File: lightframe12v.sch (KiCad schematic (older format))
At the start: 43 parts, among them J1 PJ-077, J2 Conn_01x06_Female, J3 Conn_01x02_Female, J4 Conn_01x06_Female, J5 Conn_01x04_Female, J6 Conn_01x6_Female, Q1 MMBT2222A-TP, Q2 MMBT2222A-TP, SW1 SW_Push, SW2 SW_Push, U1 TPS562211, U2 ESP32-WROOM-32U, U3 TLC5971

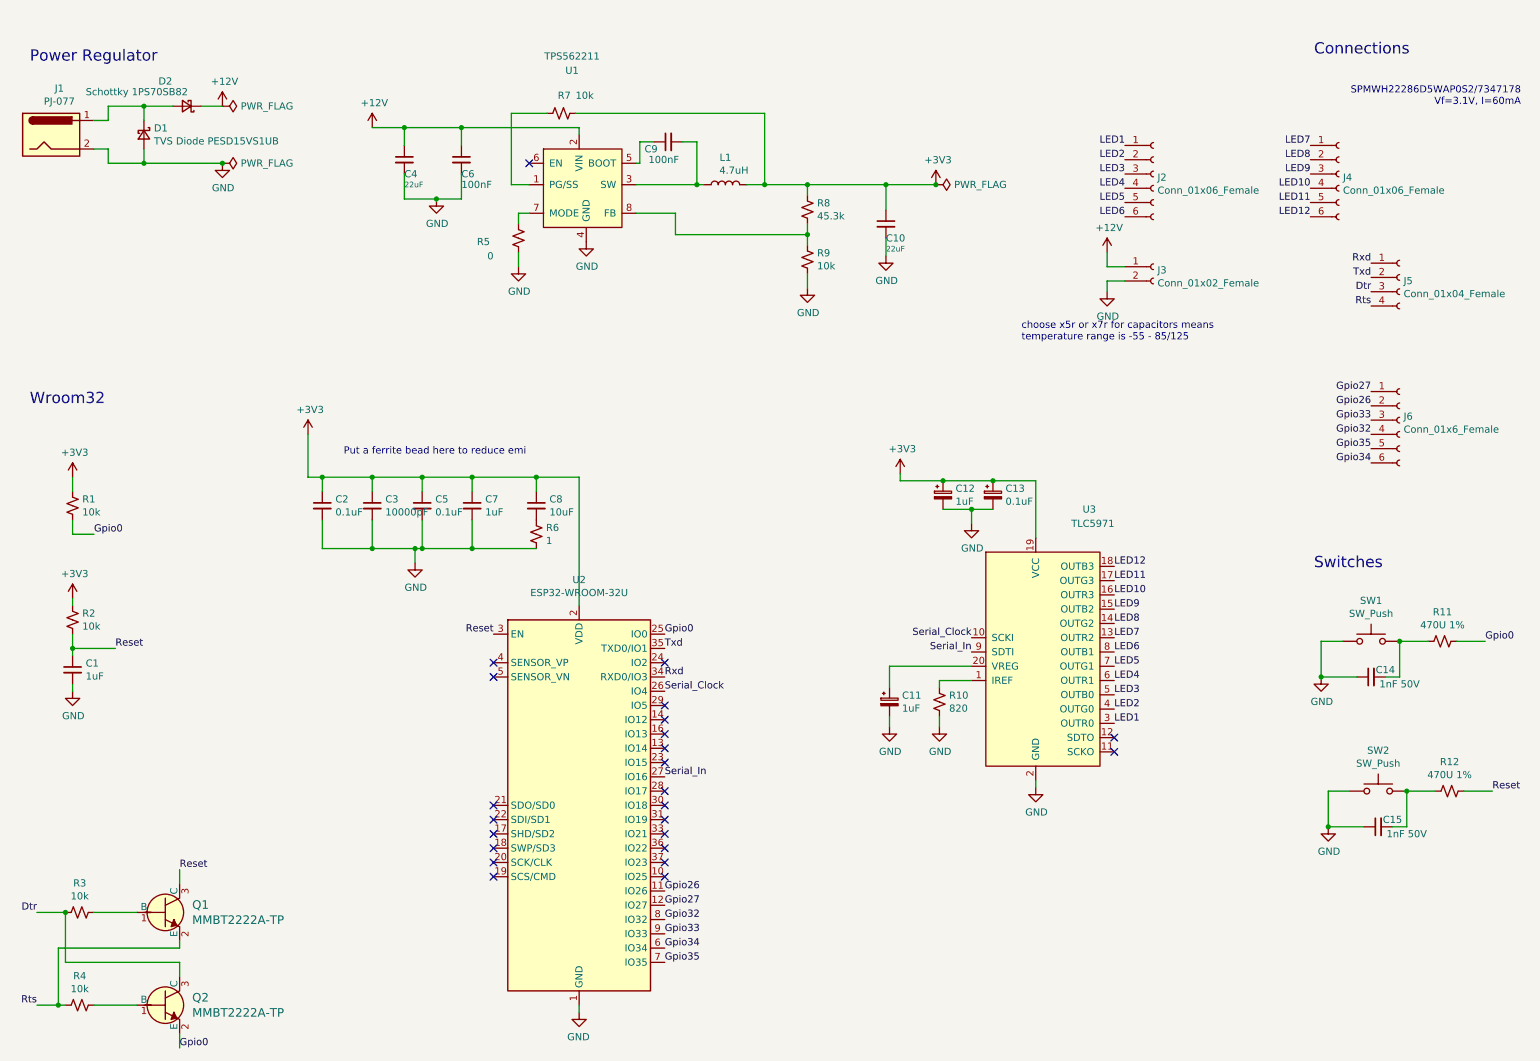
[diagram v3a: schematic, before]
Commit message: Top ground plane with cutouts.
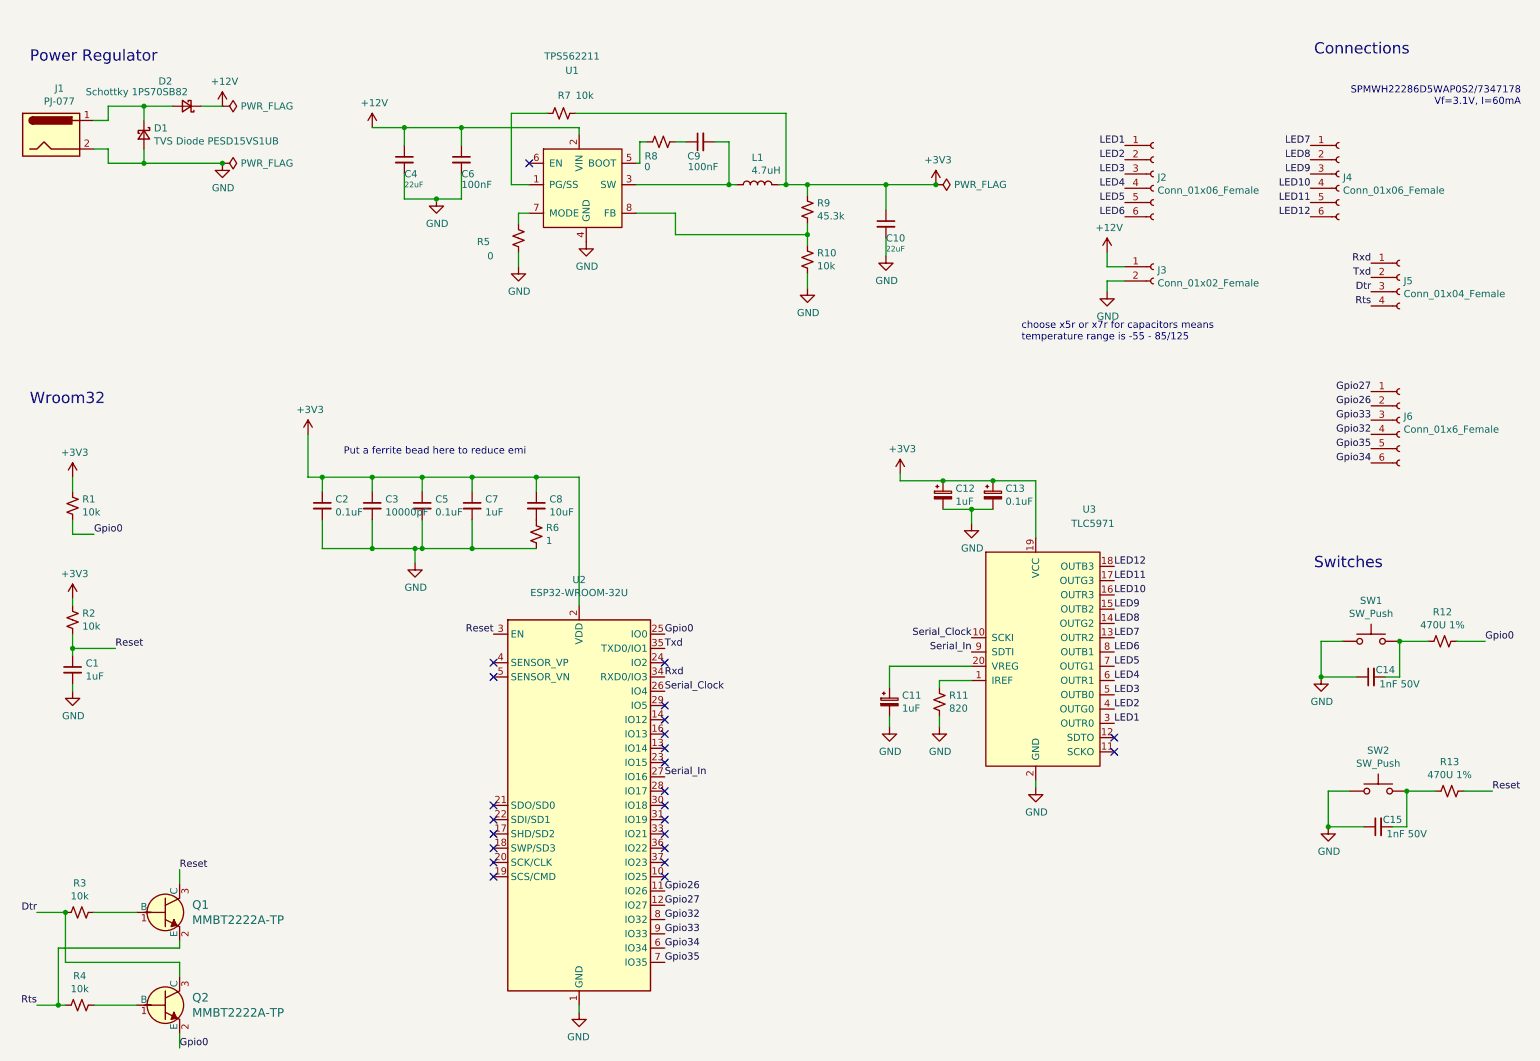
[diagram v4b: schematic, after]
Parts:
- added R8: 0, digikey-footprints:0603, symbol Device:R_Small_US
- R10: renamed from R9; footprint Resistor_SMD:R_0402_1005Metric -> digikey-footprints:0603
- R9: renamed from R8; footprint Resistor_SMD:R_0402_1005Metric -> digikey-footprints:0603
- renumbered R10 to R11, R11 to R12, R12 to R13
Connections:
- net at U1.5 (BOOT): now also R8.1; no longer C9.1
- new net: C9.1, R8.2
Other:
- moved on the sheet: C9, L1
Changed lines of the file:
@@
 $EndComp
 $Comp
-L Device:R_Small_US R12
+L Device:R_Small_US R13
 U 1 1 602DA52D
 P 10650 5850
-F 0 "R12" V 10855 5850 50  0000 C CNN
+F 0 "R13" V 10855 5850 50  0000 C CNN
 F 1 "470U 1%" V 10764 5850 50  0000 C CNN
 F 2 "digikey-footprints:0603" H 10650 5850 50  0001 C CNN
@@
 $EndComp
 $Comp
-L Device:R_Small_US R11
+L Device:R_Small_US R12
 U 1 1 6029A6D9
 P 10600 4800
-F 0 "R11" V 10805 4800 50  0000 C CNN
+F 0 "R12" V 10805 4800 50  0000 C CNN
 F 1 "470U 1%" V 10714 4800 50  0000 C CNN
 F 2 "digikey-footprints:0603" H 10600 4800 50  0001 C CNN
@@
 LED12
 $Comp
-L Device:R_Small_US R10
+L Device:R_Small_US R11
 U 1 1 60526411
 P 7075 5225
-F 0 "R10" H 7143 5271 50  0000 L CNN
+F 0 "R11" H 7143 5271 50  0000 L CNN
 F 1 "820" H 7143 5180 50  0000 L CNN
 F 2 "digikey-footprints:0603" H 7075 5225 50  0001 C CNN
@@
 $EndComp
 $Comp
-L Device:R_Small_US R8
+L Device:R_Small_US R9
 U 1 1 605822D2
 P 6150 1775
-F 0 "R8" H 6218 1821 50  0000 L CNN
+F 0 "R9" H 6218 1821 50  0000 L CNN
 F 1 "45.3k" H 6218 1730 50  0000 L CNN
-F 2 "Resistor_SMD:R_0402_1005Metric" H 6150 1775 50  0001 C CNN
+F 2 "digikey-footprints:0603" H 6150 1775 50  0001 C CNN
 F 3 "~" H 6150 1775 50  0001 C CNN
 	1    6150 1775
@@
 	1750 6950 1750 6900
 $Comp
-L Device:L L1
-U 1 1 6057B6D3
-P 5575 1600
-F 0 "L1" V 5765 1600 50  0000 C CNN
-F 1 "4.7uH" V 5675 1540 50  0000 C CNN
-F 2 "Keith:SRN8040 Bournes" H 5575 1600 50  0001 C CNN
-F 3 "~" H 5575 1600 50  0001 C CNN
-	1    5575 1600
-	0    -1   -1   0
-$EndComp
-$Comp
-L Device:R_Small_US R9
+L Device:R_Small_US R10
 U 1 1 6058B282
 P 6150 2125
-F 0 "R9" H 6218 2171 50  0000 L CNN
+F 0 "R10" H 6218 2171 50  0000 L CNN
 F 1 "10k" H 6218 2080 50  0000 L CNN
-F 2 "Resistor_SMD:R_0402_1005Metric" H 6150 2125 50  0001 C CNN
+F 2 "digikey-footprints:0603" H 6150 2125 50  0001 C CNN
 F 3 "~" H 6150 2125 50  0001 C CNN
 	1    6150 2125
@@
 Wire Wire Line
 	6150 1600 6700 1600
-Connection ~ 6150 1600
 Wire Wire Line
 	6700 1775 6700 1600
@@
 $EndComp
 Wire Wire Line
-	5725 1600 5850 1600
-Wire Wire Line
-	4525 1100 5850 1100
+	4525 1100 6000 1100
 Wire Wire Line
 	4075 1100 4325 1100
@@
 $EndComp
 Wire Wire Line
-	4950 1600 5375 1600
-Wire Wire Line
-	5275 1300 5375 1300
-$Comp
-L Device:C_Small C9
-U 1 1 60570E44
-P 5175 1300
-F 0 "C9" V 5125 1375 50  0000 L CNN
-F 1 "100nF" V 5050 1225 50  0000 L CNN
-F 2 "digikey-footprints:0805" H 5175 1300 50  0001 C CNN
-F 3 "~" H 5175 1300 50  0001 C CNN
-	1    5175 1300
-	0    -1   -1   0
-$EndComp
-Wire Wire Line
 	4975 1450 4975 1300
 Wire Wire Line
-	4975 1300 5075 1300
-Wire Wire Line
-	5375 1300 5375 1600
-Connection ~ 5375 1600
-Wire Wire Line
-	5375 1600 5425 1600
-Wire Wire Line
 	4075 1100 4075 1600
 Wire Wire Line
@@
 Wire Wire Line
 	4550 1250 4550 1200
-Wire Wire Line
-	5850 1100 5850 1600
-Connection ~ 5850 1600
-Wire Wire Line
-	5850 1600 6150 1600
 $Comp
 L power:+12V #PWR021
@@
 	1    0    0    -1
 $EndComp
+$Comp
+L Device:R_Small_US R8
+U 1 1 605B65C7
+P 5125 1300
+F 0 "R8" V 5025 1325 50  0000 L CNN
+F 1 "0" V 4950 1375 50  0000 L CNN
+F 2 "digikey-footprints:0603" H 5125 1300 50  0001 C CNN
+F 3 "~" H 5125 1300 50  0001 C CNN
+	1    5125 1300
+	0    -1   -1   0
+$EndComp
+Wire Wire Line
+	4975 1300 5025 1300
+Wire Wire Line
+	5225 1300 5300 1300
+$Comp
+L Device:L L1
+U 1 1 6057B6D3
+P 5800 1600
+F 0 "L1" V 5990 1600 50  0000 C CNN
+F 1 "4.7uH" V 5900 1540 50  0000 C CNN
+F 2 "Keith:SRN8040 Bournes" H 5800 1600 50  0001 C CNN
+F 3 "~" H 5800 1600 50  0001 C CNN
+	1    5800 1600
+	0    -1   -1   0
+$EndComp
+Wire Wire Line
+	5950 1600 6000 1600
+Connection ~ 6150 1600
+Wire Wire Line
+	6000 1100 6000 1600
+Connection ~ 6000 1600
+Wire Wire Line
+	6000 1600 6150 1600
+Wire Wire Line
+	4950 1600 5600 1600
+Wire Wire Line
+	5500 1300 5600 1300
+Wire Wire Line
+	5600 1300 5600 1600
+$Comp
+L Device:C_Small C9
+U 1 1 60570E44
+P 5400 1300
+F 0 "C9" V 5300 1300 50  0000 L CNN
+F 1 "100nF" V 5225 1175 50  0000 L CNN
+F 2 "digikey-footprints:0805" H 5400 1300 50  0001 C CNN
+F 3 "~" H 5400 1300 50  0001 C CNN
+	1    5400 1300
+	0    -1   -1   0
+$EndComp
+Wire Wire Line
+	5650 1600 5600 1600
+Connection ~ 5600 1600
 $EndSCHEMATC

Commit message: Pmic refactor.
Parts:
- added TP1: wall in, TestPoint:TestPoint_Pad_1.5x1.5mm, symbol Connector:TestPoint_Small
- added TP3: pgss, TestPoint:TestPoint_Pad_1.5x1.5mm, symbol Connector:TestPoint_Small
- added TP4: 3v3 out, TestPoint:TestPoint_Pad_1.5x1.5mm, symbol Connector:TestPoint_Small
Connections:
- net +12V: now also TP1.1
- net +3V3: now also TP4.1
- net at R7.2, U1.1 (PG/SS): now also TP3.1
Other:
- moved on the sheet: C10, C4, C6, C9, D1, D2, J1, L1, R10, R5, R7, R8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

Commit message: More layout.
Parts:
- removed J3: Conn_01x02_Female, Connector_PinSocket_2.54mm:PinSocket_1x02_P2.54mm_Vertical, symbol Connector:Conn_01x02_Female
- added TP2: ground test, TestPoint:TestPoint_Pad_1.5x1.5mm, symbol Connector:TestPoint_Small
- J2, J4: value Conn_01x06_Female -> Conn_01x07_Female; footprint Connector_PinSocket_2.54mm:PinSocket_1x06_P2.54mm_Vertical -> Connector_PinHeader_2.54mm:PinHeader_1x07_P2.54mm_Vertical; symbol Connector:Conn_01x06_Female -> Connector:Conn_01x07_Female
- J6: value Conn_01x6_Female -> Conn_01x4_Female; footprint Connector_PinSocket_2.54mm:PinSocket_1x06_P2.54mm_Vertical -> Connector_PinHeader_2.54mm:PinHeader_1x04_P2.54mm_Vertical; symbol Connector:Conn_01x06_Female -> Connector:Conn_01x04_Female
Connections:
- net +12V: now also J2.7 (Pin_7), J4.7 (Pin_7)
- net Dtr: now also Q2.2 (E); no longer Q2.3 (C)
- net GND: now also TP2.1
- net Gpio0: now also Q2.3 (C); no longer Q2.2 (E)
- net Gpio34: now also J6.4 (Pin_4); no longer J6.6 (Pin_6)
- net Gpio35: now also J6.3 (Pin_3); no longer J6.5 (Pin_5)
- net Serial_Clock: now also U2.9 (IO33); no longer U2.26 (IO4)
- net Serial_In: now also U2.8 (IO32); no longer U2.27 (IO16)
- removed net Gpio32: J6.4 (Pin_4), U2.8 (IO32)
- removed net Gpio33: J6.3 (Pin_3), U2.9 (IO33)
- no-connect marks 24 -> 26

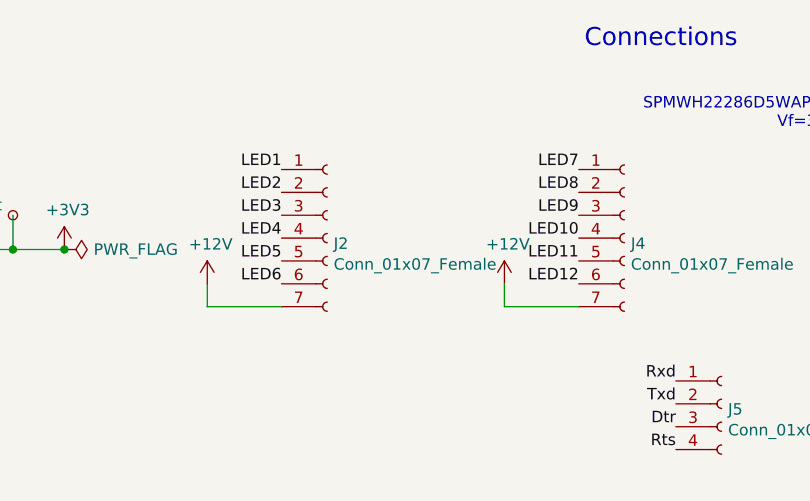
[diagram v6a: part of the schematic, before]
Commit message: Plane cleanup and power rails.
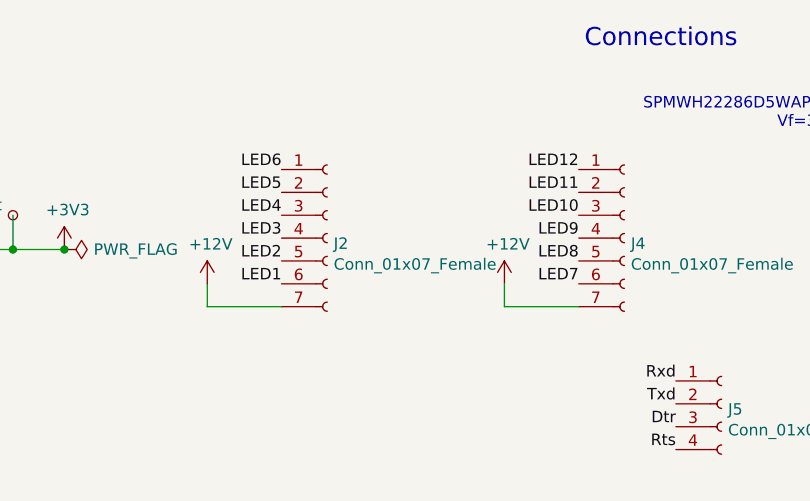
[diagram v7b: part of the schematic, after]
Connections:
- net LED1: now also J2.6 (Pin_6); no longer J2.1 (Pin_1)
- net LED10: now also J4.3 (Pin_3); no longer J4.4 (Pin_4)
- net LED11: now also J4.2 (Pin_2); no longer J4.5 (Pin_5)
- net LED12: now also J4.1 (Pin_1); no longer J4.6 (Pin_6)
- net LED2: now also J2.5 (Pin_5); no longer J2.2 (Pin_2)
- net LED3: now also J2.4 (Pin_4); no longer J2.3 (Pin_3)
- net LED4: now also J2.3 (Pin_3); no longer J2.4 (Pin_4)
- net LED5: now also J2.2 (Pin_2); no longer J2.5 (Pin_5)
- net LED6: now also J2.1 (Pin_1); no longer J2.6 (Pin_6)
- net LED7: now also J4.6 (Pin_6); no longer J4.1 (Pin_1)
- net LED8: now also J4.5 (Pin_5); no longer J4.2 (Pin_2)
- net LED9: now also J4.4 (Pin_4); no longer J4.3 (Pin_3)
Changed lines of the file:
@@
 NoConn ~ 8300 5475
 NoConn ~ 8300 5575
+Text Label 8375 1725 2    50   ~ 0
+LED1
+Text Label 8375 1625 2    50   ~ 0
+LED2
+Text Label 8375 1525 2    50   ~ 0
+LED3
+Text Label 8375 1425 2    50   ~ 0
+LED4
+Text Label 8375 1325 2    50   ~ 0
+LED5
 Text Label 8375 1225 2    50   ~ 0
-LED1
-Text Label 8375 1325 2    50   ~ 0
-LED2
-Text Label 8375 1425 2    50   ~ 0
-LED3
-Text Label 8375 1525 2    50   ~ 0
-LED4
-Text Label 8375 1625 2    50   ~ 0
-LED5
-Text Label 8375 1725 2    50   ~ 0
 LED6
 $Comp
@@
 	1    0    0    -1
 $EndComp
+Text Label 9675 1725 2    50   ~ 0
+LED7
+Text Label 9675 1625 2    50   ~ 0
+LED8
+Text Label 9675 1525 2    50   ~ 0
+LED9
+Text Label 9675 1425 2    50   ~ 0
+LED10
+Text Label 9675 1325 2    50   ~ 0
+LED11
 Text Label 9675 1225 2    50   ~ 0
-LED7
-Text Label 9675 1325 2    50   ~ 0
-LED8
-Text Label 9675 1425 2    50   ~ 0
-LED9
-Text Label 9675 1525 2    50   ~ 0
-LED10
-Text Label 9675 1625 2    50   ~ 0
-LED11
-Text Label 9675 1725 2    50   ~ 0
 LED12
 Text Label 8300 5375 0    50   ~ 0
